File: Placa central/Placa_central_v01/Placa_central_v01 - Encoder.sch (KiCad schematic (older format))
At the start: 20 parts, among them J1 Conn_01x01_Female, J2 Conn_01x01_Female, J3 Conn_01x01_Female, J4 Conn_01x01_Female, J5 Conn_01x01_Female, J6 Conn_01x01_Female, U1 TCRT5000Esq, U2 LM741Esq, U3 TCRT5000Dir, U4 LM741

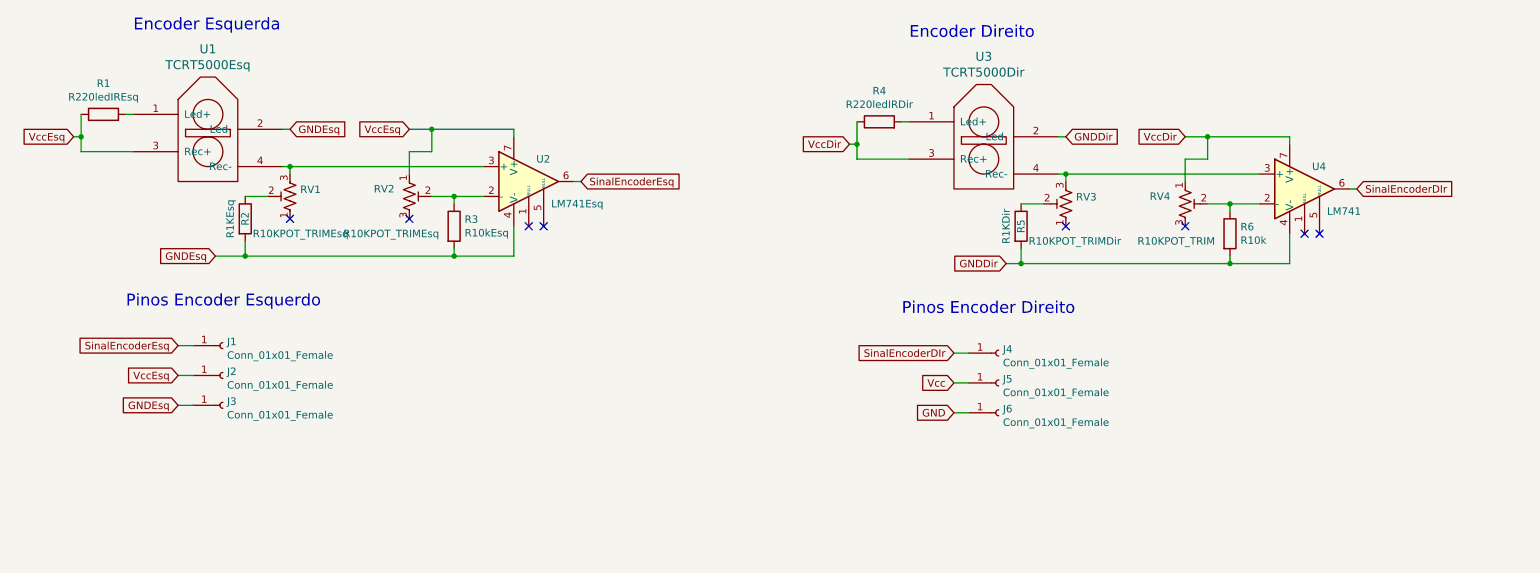
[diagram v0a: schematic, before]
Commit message: Adicionado Furos a placa encoder. Falta root
Adicionados os furos do suporte para o andar superior e para fixação no case do motor. Falta root
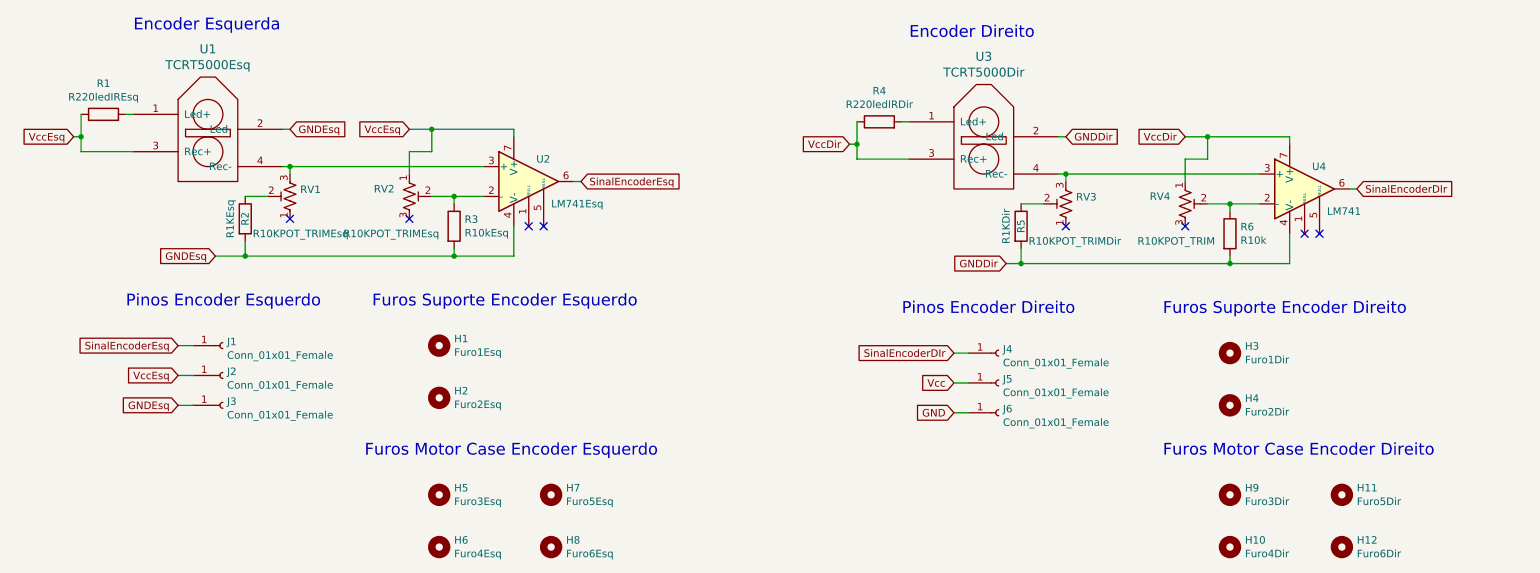
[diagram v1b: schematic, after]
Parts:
- added H1: Furo1Esq, MountingHole:MountingHole_3mm, symbol Mechanical:MountingHole
- added H10: Furo4Dir, MountingHole:MountingHole_2mm, symbol Mechanical:MountingHole
- added H11: Furo5Dir, MountingHole:MountingHole_2mm, symbol Mechanical:MountingHole
- added H12: Furo6Dir, MountingHole:MountingHole_2mm, symbol Mechanical:MountingHole
- added H2: Furo2Esq, MountingHole:MountingHole_3mm, symbol Mechanical:MountingHole
- added H3: Furo1Dir, MountingHole:MountingHole_3mm, symbol Mechanical:MountingHole
- added H4: Furo2Dir, MountingHole:MountingHole_3mm, symbol Mechanical:MountingHole
- added H5: Furo3Esq, MountingHole:MountingHole_2mm, symbol Mechanical:MountingHole
- added H6: Furo4Esq, MountingHole:MountingHole_2mm, symbol Mechanical:MountingHole
- added H7: Furo5Esq, MountingHole:MountingHole_2mm, symbol Mechanical:MountingHole
- added H8: Furo6Esq, MountingHole:MountingHole_2mm, symbol Mechanical:MountingHole
- added H9: Furo3Dir, MountingHole:MountingHole_2mm, symbol Mechanical:MountingHole
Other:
- note added: "Furos Motor Case Encoder Direito"
- note added: "Furos Motor Case Encoder Esquerdo"
- note added: "Furos Suporte Encoder Direito"
- note added: "Furos Suporte Encoder Esquerdo"
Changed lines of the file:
@@
 Text GLabel 7650 3000 0    50   Input ~ 0
 GNDDir
+Text Notes 3400 3300 0    79   ~ 0
+Furos Suporte Encoder Esquerdo
+$Comp
+L Mechanical:MountingHole H1
+U 1 1 5D406AF8
+P 3850 3550
+F 0 "H1" H 3950 3596 50  0000 L CNN
+F 1 "Furo1Esq" H 3950 3505 50  0000 L CNN
+F 2 "MountingHole:MountingHole_3mm" H 3850 3550 50  0001 C CNN
+F 3 "~" H 3850 3550 50  0001 C CNN
+	1    3850 3550
+	1    0    0    -1
+$EndComp
+$Comp
+L Mechanical:MountingHole H2
+U 1 1 5D4070A4
+P 3850 3900
+F 0 "H2" H 3950 3946 50  0000 L CNN
+F 1 "Furo2Esq" H 3950 3855 50  0000 L CNN
+F 2 "MountingHole:MountingHole_3mm" H 3850 3900 50  0001 C CNN
+F 3 "~" H 3850 3900 50  0001 C CNN
+	1    3850 3900
+	1    0    0    -1
+$EndComp
+Text Notes 8700 3350 0    79   ~ 0
+Furos Suporte Encoder Direito
+$Comp
+L Mechanical:MountingHole H3
+U 1 1 5D407741
+P 9150 3600
+F 0 "H3" H 9250 3646 50  0000 L CNN
+F 1 "Furo1Dir" H 9250 3555 50  0000 L CNN
+F 2 "MountingHole:MountingHole_3mm" H 9150 3600 50  0001 C CNN
+F 3 "~" H 9150 3600 50  0001 C CNN
+	1    9150 3600
+	1    0    0    -1
+$EndComp
+$Comp
+L Mechanical:MountingHole H4
+U 1 1 5D40774B
+P 9150 3950
+F 0 "H4" H 9250 3996 50  0000 L CNN
+F 1 "Furo2Dir" H 9250 3905 50  0000 L CNN
+F 2 "MountingHole:MountingHole_3mm" H 9150 3950 50  0001 C CNN
+F 3 "~" H 9150 3950 50  0001 C CNN
+	1    9150 3950
+	1    0    0    -1
+$EndComp
+Text Notes 3350 4300 0    79   ~ 0
+Furos Motor Case Encoder Esquerdo
+Text Notes 8700 4300 0    79   ~ 0
+Furos Motor Case Encoder Direito
+$Comp
+L Mechanical:MountingHole H5
+U 1 1 5D40CB8F
+P 3850 4550
+F 0 "H5" H 3950 4596 50  0000 L CNN
+F 1 "Furo3Esq" H 3950 4505 50  0000 L CNN
+F 2 "MountingHole:MountingHole_2mm" H 3850 4550 50  0001 C CNN
+F 3 "~" H 3850 4550 50  0001 C CNN
+	1    3850 4550
+	1    0    0    -1
+$EndComp
+$Comp
+L Mechanical:MountingHole H6
+U 1 1 5D40CB95
+P 3850 4900
+F 0 "H6" H 3950 4946 50  0000 L CNN
+F 1 "Furo4Esq" H 3950 4855 50  0000 L CNN
+F 2 "MountingHole:MountingHole_2mm" H 3850 4900 50  0001 C CNN
+F 3 "~" H 3850 4900 50  0001 C CNN
+	1    3850 4900
+	1    0    0    -1
+$EndComp
+$Comp
+L Mechanical:MountingHole H7
+U 1 1 5D40DDE5
+P 4600 4550
+F 0 "H7" H 4700 4596 50  0000 L CNN
+F 1 "Furo5Esq" H 4700 4505 50  0000 L CNN
+F 2 "MountingHole:MountingHole_2mm" H 4600 4550 50  0001 C CNN
+F 3 "~" H 4600 4550 50  0001 C CNN
+	1    4600 4550
+	1    0    0    -1
+$EndComp
+$Comp
+L Mechanical:MountingHole H8
+U 1 1 5D40DDEB
+P 4600 4900
+F 0 "H8" H 4700 4946 50  0000 L CNN
+F 1 "Furo6Esq" H 4700 4855 50  0000 L CNN
+F 2 "MountingHole:MountingHole_2mm" H 4600 4900 50  0001 C CNN
+F 3 "~" H 4600 4900 50  0001 C CNN
+	1    4600 4900
+	1    0    0    -1
+$EndComp
+$Comp
+L Mechanical:MountingHole H9
+U 1 1 5D40EB57
+P 9150 4550
+F 0 "H9" H 9250 4596 50  0000 L CNN
+F 1 "Furo3Dir" H 9250 4505 50  0000 L CNN
+F 2 "MountingHole:MountingHole_2mm" H 9150 4550 50  0001 C CNN
+F 3 "~" H 9150 4550 50  0001 C CNN
+	1    9150 4550
+	1    0    0    -1
+$EndComp
+$Comp
+L Mechanical:MountingHole H10
+U 1 1 5D40EB61
+P 9150 4900
+F 0 "H10" H 9250 4946 50  0000 L CNN
+F 1 "Furo4Dir" H 9250 4855 50  0000 L CNN
+F 2 "MountingHole:MountingHole_2mm" H 9150 4900 50  0001 C CNN
+F 3 "~" H 9150 4900 50  0001 C CNN
+	1    9150 4900
+	1    0    0    -1
+$EndComp
+$Comp
+L Mechanical:MountingHole H11
+U 1 1 5D40EB6B
+P 9900 4550
+F 0 "H11" H 10000 4596 50  0000 L CNN
+F 1 "Furo5Dir" H 10000 4505 50  0000 L CNN
+F 2 "MountingHole:MountingHole_2mm" H 9900 4550 50  0001 C CNN
+F 3 "~" H 9900 4550 50  0001 C CNN
+	1    9900 4550
+	1    0    0    -1
+$EndComp
+$Comp
+L Mechanical:MountingHole H12
+U 1 1 5D40EB75
+P 9900 4900
+F 0 "H12" H 10000 4946 50  0000 L CNN
+F 1 "Furo6Dir" H 10000 4855 50  0000 L CNN
+F 2 "MountingHole:MountingHole_2mm" H 9900 4900 50  0001 C CNN
+F 3 "~" H 9900 4900 50  0001 C CNN
+	1    9900 4900
+	1    0    0    -1
+$EndComp
 $EndSCHEMATC

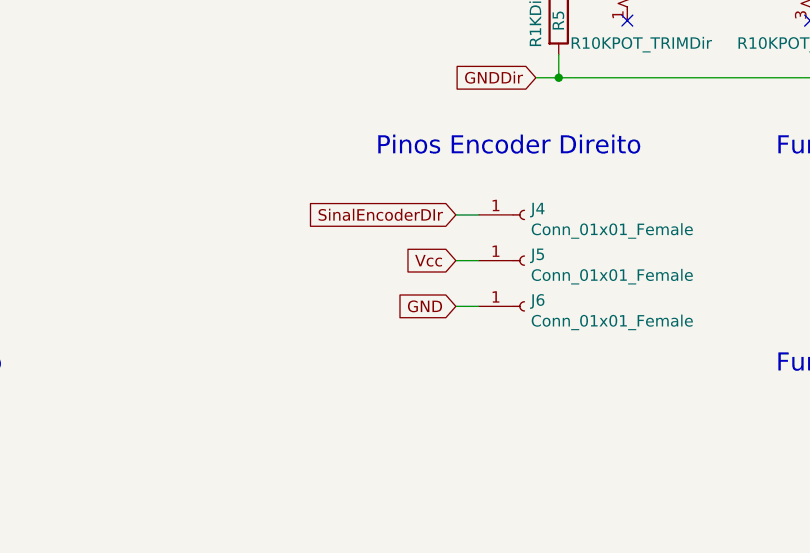
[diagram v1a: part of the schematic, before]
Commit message: Tentativa de root placa de encoder
placa da direita rooteada e a placa da esquerda em processo.
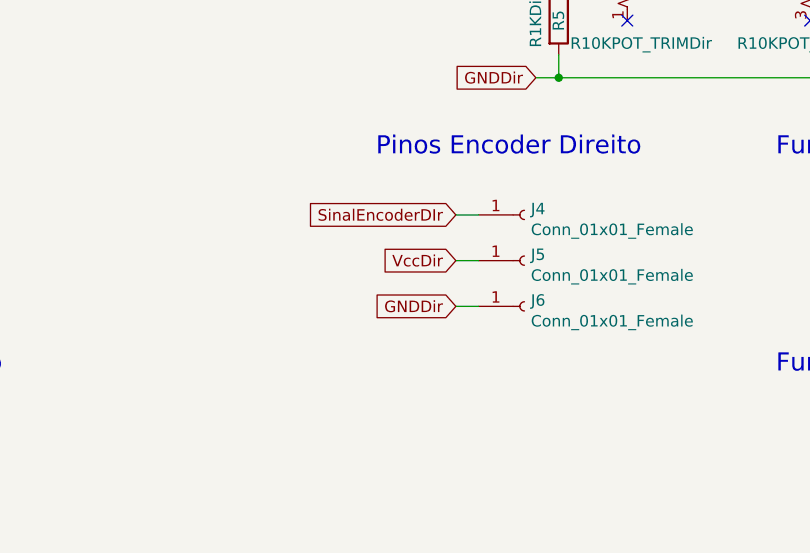
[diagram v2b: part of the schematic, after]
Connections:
- net GND is gone; now on net GNDDir: J6.1 (Pin_1)
- net Vcc is gone; now on net VccDir: J5.1 (Pin_1)
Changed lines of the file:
@@
 $EndComp
 Text GLabel 7300 4000 0    50   Input ~ 0
-GND
+GNDDir
 Text GLabel 7300 3600 0    50   Input ~ 0
 SinalEncoderDIr
@@
 VccDir
 Text GLabel 7300 3800 0    50   Input ~ 0
-Vcc
+VccDir
 Wire Wire Line
 	6600 2200 6650 2200
